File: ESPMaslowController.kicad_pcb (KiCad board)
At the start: 2 copper layers, 80 x 100 mm, 60 parts, among them J1 Barrel_Jack_Switch, J10 Conn_01x03, J11 Conn_01x03, J2 B6B-PH-K-S, J3 B6B-PH-K-S, J4 B6B-PH-K-S, J5 B6B-PH-K-S, J6 B6B-PH-K-S, J7 Micro_SD_Card_Det, J8 Conn_01x03, J9 Conn_02x12_Odd_Even, U1 NCP3063, U2 ESP32-DevKit-Doit, U3 ATmega328PB-AU, U4 IFX9201, U5 IFX9201, U6 IFX9201, U7 IFX9201, U8 IFX9201

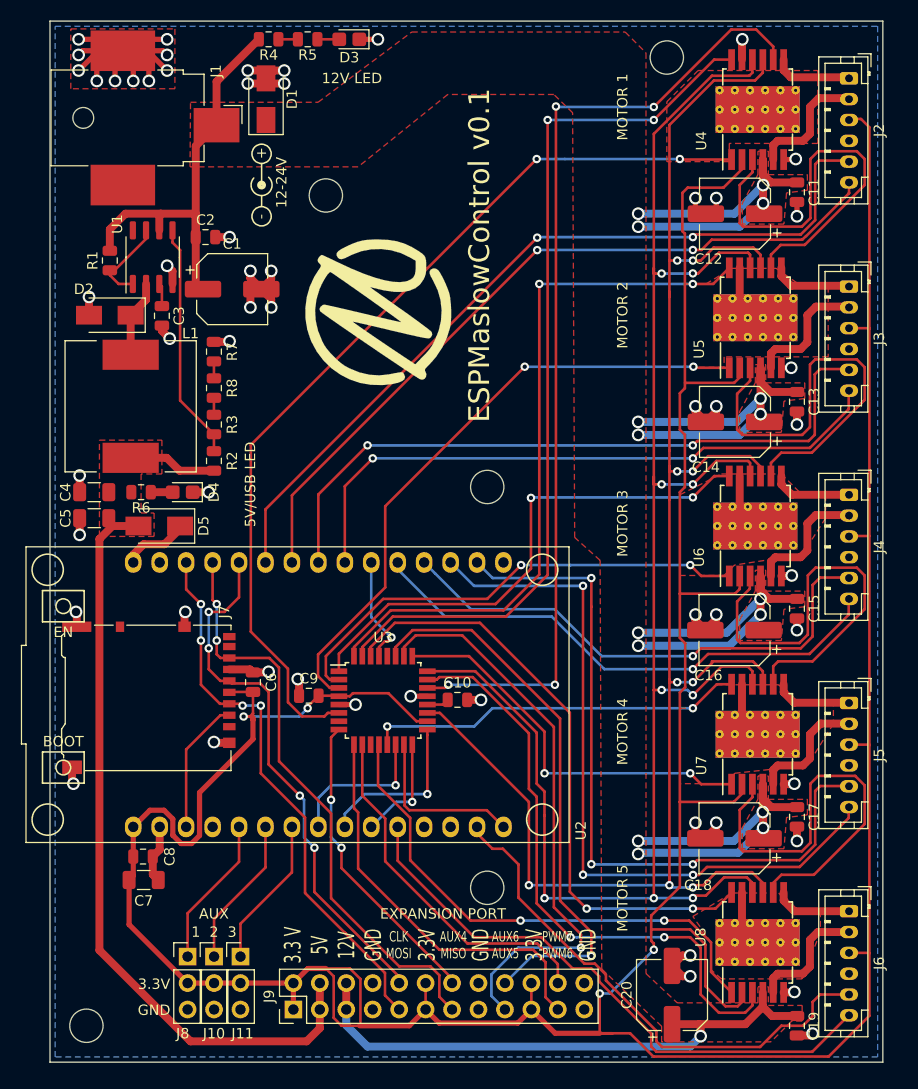
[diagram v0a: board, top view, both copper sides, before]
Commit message: Added pullups to unused SD card lines.
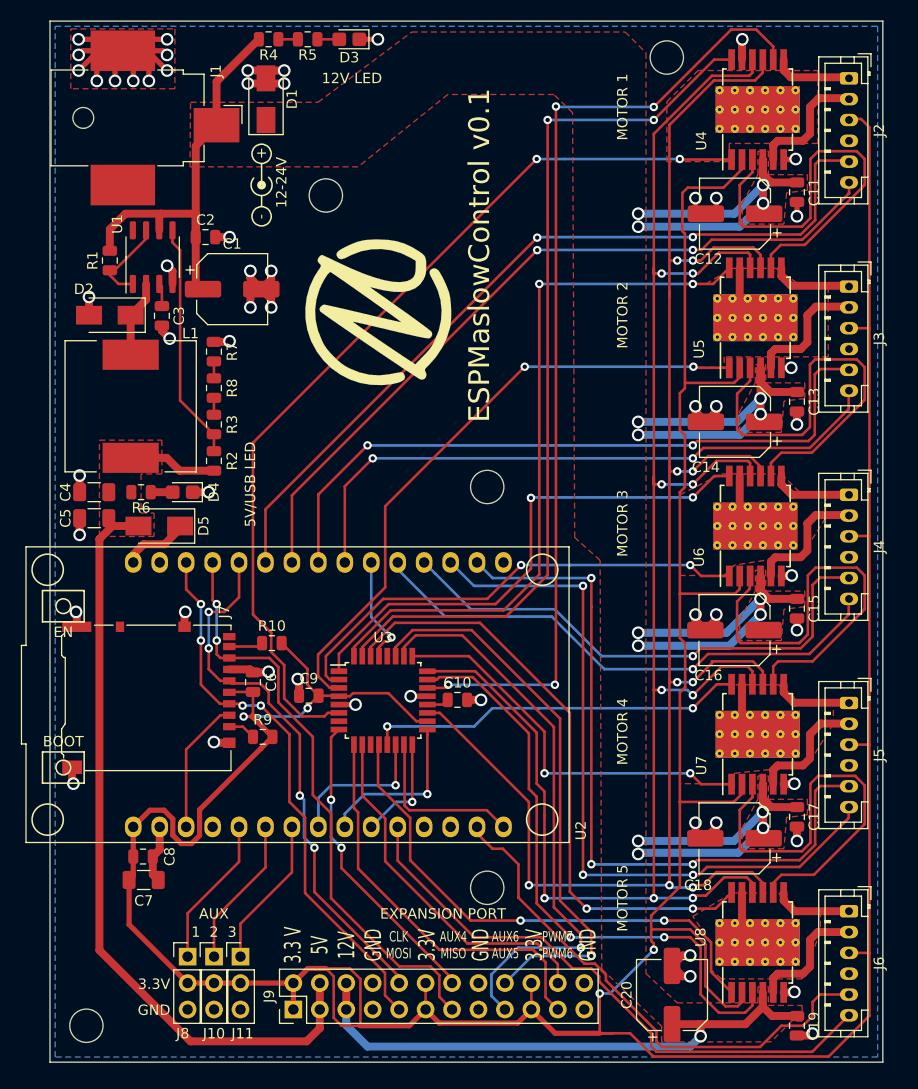
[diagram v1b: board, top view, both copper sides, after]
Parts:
- added R10: 10K, Resistor_SMD:R_0805_2012Metric, F.Cu at (117.3, 119.8)
- added R9: 10K, Resistor_SMD:R_0805_2012Metric, F.Cu at (116.4, 128.8)
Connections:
- J7 pad 1: (no net) -> Net-(J7-Pad1)
- J7 pad 8: (no net) -> Net-(J7-Pad8)
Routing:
- net +3V3: track 393.8 -> 401.6 mm
- net Net-(J7-Pad8): track 0.00 -> 3.28 mm
- net Net-(J7-Pad1): track 0.00 -> 2.68 mm

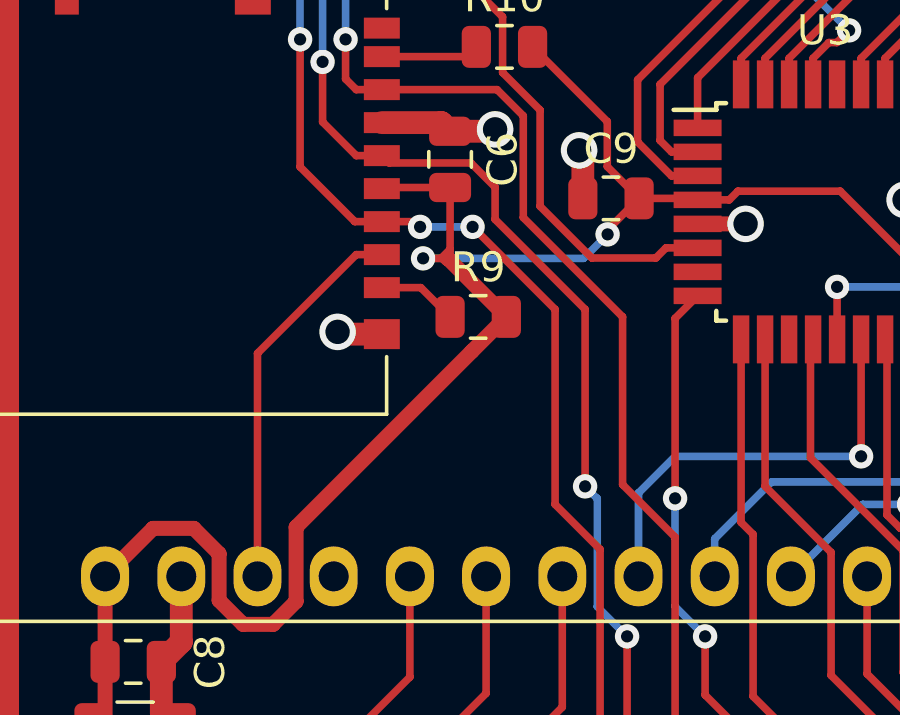
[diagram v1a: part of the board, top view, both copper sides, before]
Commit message: Added pullup to SD CS line.
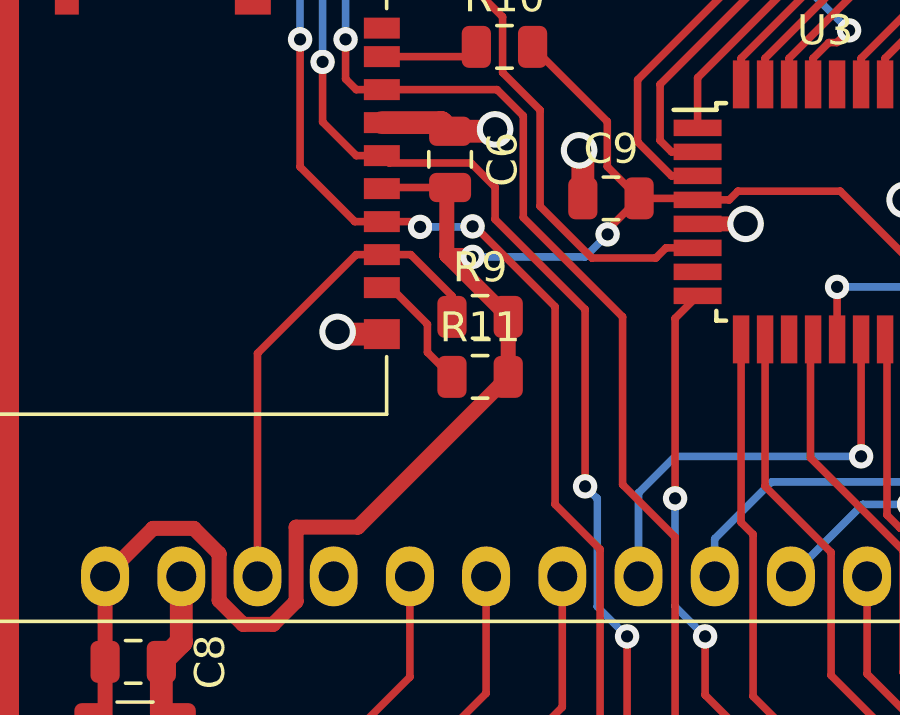
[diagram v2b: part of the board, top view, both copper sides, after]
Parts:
- added R11: 10K, Resistor_SMD:R_0805_2012Metric, F.Cu at (116.5, 130.8)
- moved R9 0.06 mm to (116.5, 128.8)
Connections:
- R9 pad 1: Net-(J7-Pad1) -> /SD_CS
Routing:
- net /SD_CS: track 12.9 -> 16.5 mm
- net Net-(J7-Pad1): track 2.68 -> 4.12 mm
- net +3V3: track 401.6 -> 400.8 mm

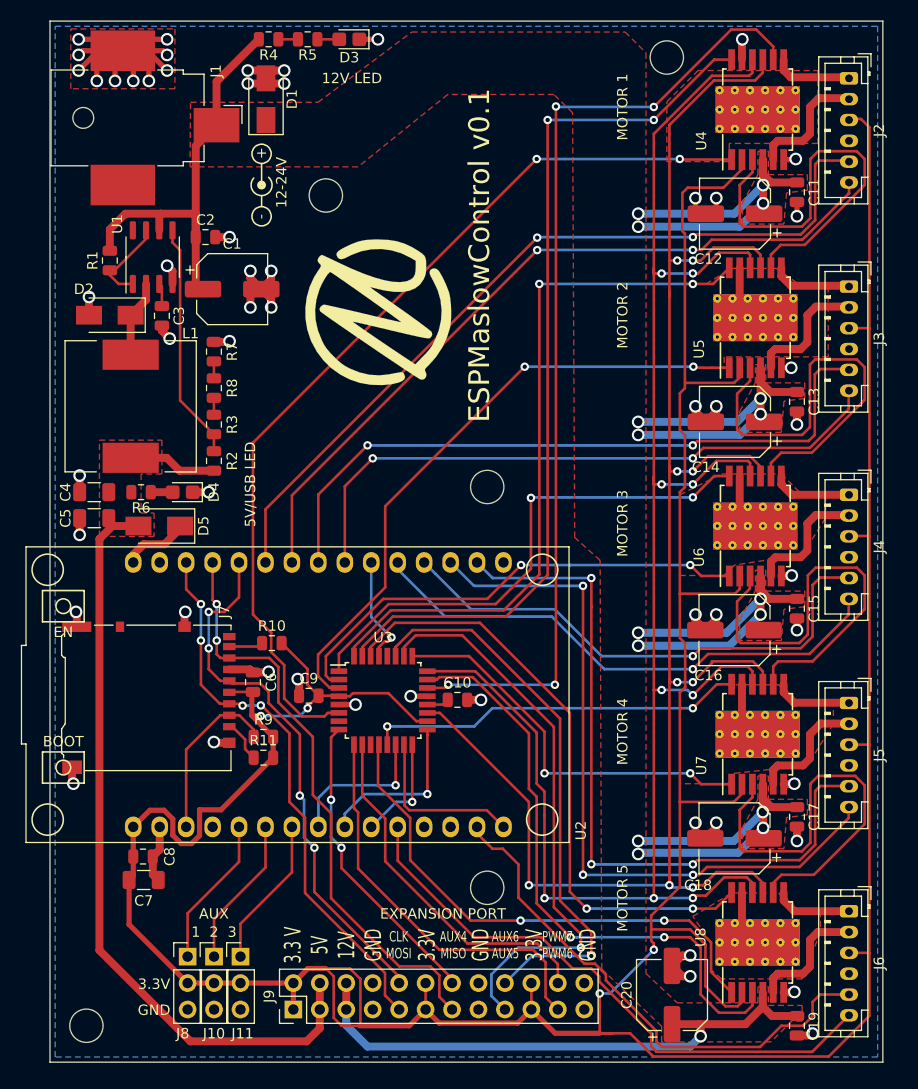
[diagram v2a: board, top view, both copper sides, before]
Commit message: Fixed board errors.
Corrected motor connectors to be JST XH series (2.5 mm pitch).
Corrected NCP3063 feedback resistor divider for 5V output.
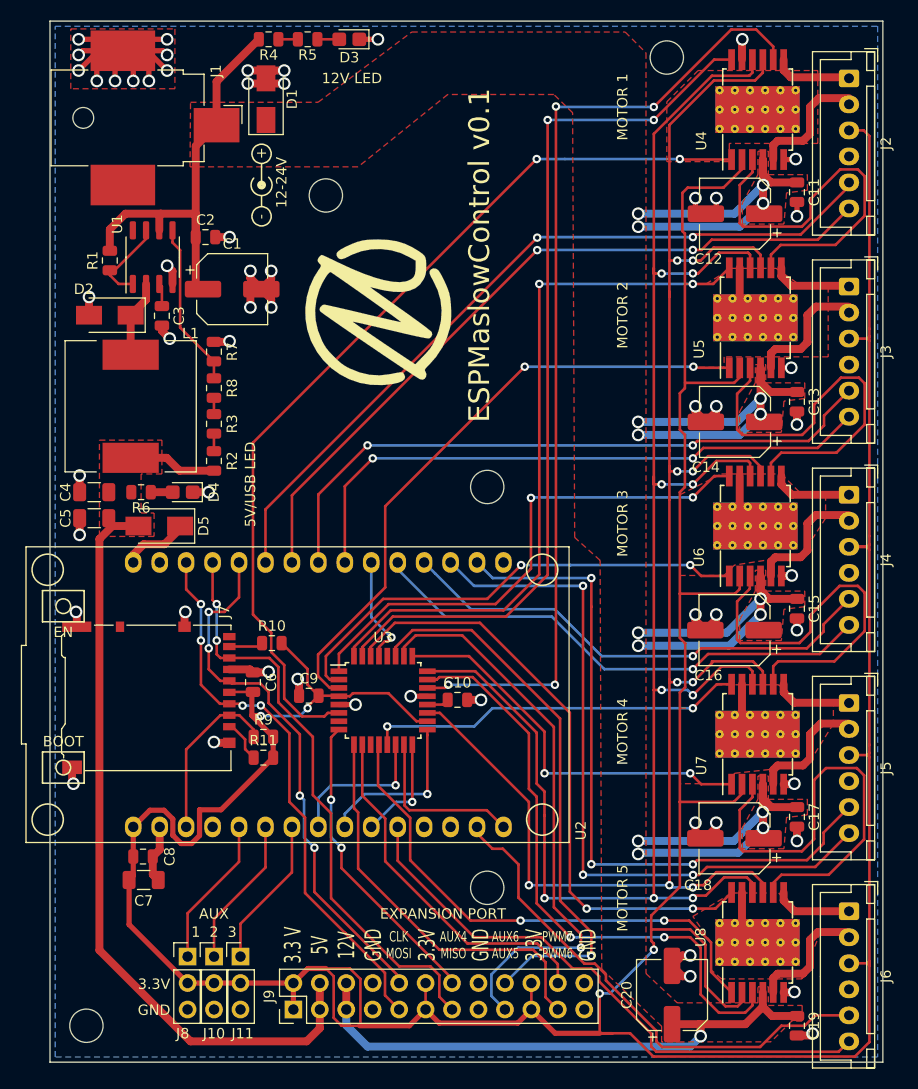
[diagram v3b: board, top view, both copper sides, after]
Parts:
- J2, J3, J4, J5, J6: value B6B-PH-K-S -> B6B-XH-A; footprint Connector_JST:JST_PH_B6B-PH-K_1x06_P2.00mm_Vertical -> Connector_JST:JST_XH_B6B-XH-A_1x06_P2.50mm_Vertical
- moved R3 0.06 mm to (111.8, 98.7), turned to 270 degrees
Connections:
- R3 pad 1: Net-(R2-Pad2) -> Net-(R3-Pad1)
- R3 pad 2: Net-(R3-Pad2) -> Net-(R2-Pad2)
- R8 pad 1: Net-(R3-Pad2) -> Net-(R3-Pad1)
- U1 pad 5: Net-(R2-Pad2) -> Net-(R7-Pad1)
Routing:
- net Net-(R2-Pad2): track 22.9 -> 1.69 mm
- net Net-(R7-Pad1): track 1.62 -> 15.9 mm
- net +3V3: track 400.8 -> 404.8 mm
- net /ENC1A: track 78.2 -> 74.4 mm
- net /ENC2A: track 65.9 -> 62.2 mm
- net /DC Driver 3/MISO: track 41.7 -> 38.1 mm
- net /DC Driver 2/MISO: track 41.6 -> 38.2 mm
- net /ENC3A: track 50.5 -> 47.2 mm
- net /ENC4A: track 70.0 -> 66.7 mm
- net /DC Driver 1/MISO: track 40.9 -> 38.0 mm
- net /ENC2B: track 60.6 -> 58.5 mm
- net /DC Driver 4/MISO: track 41.2 -> 43.2 mm
- net /ENC3B: track 51.7 -> 49.7 mm
- net /ENC4B: track 70.3 -> 68.6 mm
- net Net-(R3-Pad2): track 1.62 -> 0.00 mm
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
